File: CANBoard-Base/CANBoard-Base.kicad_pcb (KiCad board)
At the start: 4 copper layers, 62.2 x 73.8 mm, 110 parts, among them J1 DTM12 A, J2 DTM12 B, U1 CANBoard_v2, U2 LM324, U3 LM324, U4 SRV05-4, U5 SRV05-4, U6 SRV05-4, U7 SRV05-4, U8 LD1117S33CTR

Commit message: version 1.1 ready for manuf
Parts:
- moved R13 34.8 mm to (3.81, -30.8), turned to 90 degrees
- moved JP5 34.3 mm to (6.10, -30.8), turned to 90 degrees
- moved R12 33.6 mm to (8.38, -30.8), turned to 90 degrees
- moved JP4 33.3 mm to (10.7, -30.8), turned to 90 degrees
- moved R14 31.9 mm to (3.81, -34.4)
- moved JP10 31.4 mm to (6.10, -34.5), turned to -90 degrees
- moved R15 30.6 mm to (8.38, -34.4)
- moved JP9 30.2 mm to (10.7, -34.5), turned to -90 degrees
- moved R11 21.1 mm to (3.81, -21.3), turned to 90 degrees
- moved JP3 20.7 mm to (6.10, -21.3), turned to 90 degrees
- moved R16 20.6 mm to (3.81, -24.9)
- moved R10 20.1 mm to (8.38, -21.3), turned to 90 degrees
- moved JP8 20.0 mm to (6.10, -24.9), turned to -90 degrees
- moved JP2 19.7 mm to (10.7, -21.3), turned to 90 degrees
- moved R17 19.6 mm to (8.38, -24.9)
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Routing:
- net AI4_RAW: track 19.5 -> 45.8 mm
- net AI5_RAW: track 21.8 -> 45.2 mm
- net AI1_RAW: track 20.2 -> 32.1 mm
- net AI2_RAW: track 18.9 -> 30.5 mm
- net AI3_RAW: track 18.6 -> 28.9 mm
- net +5VP: track 16.1 -> 8.48 mm
- net +5V: track 55.4 -> 56.4 mm
- net Net-(JP9-A): track 2.35 -> 2.99 mm
- net Net-(JP8-A): track 2.35 -> 2.93 mm
- net Net-(JP6-A): track 2.35 -> 2.93 mm
- net Net-(JP7-A): track 2.35 -> 2.93 mm
- net Net-(JP10-A): track 2.47 -> 2.98 mm
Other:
- board text added: "1"
- board text added: "2"
- board text added: "3"
- board text added: "4"
- board text added: "5"
- board text added: "ANALOG INPUTS"
- board text added: "DIGITAL INPUTS"
- board text added: "PD"
- board text added: "PU"
- board text removed: "5|4|3|2|1"

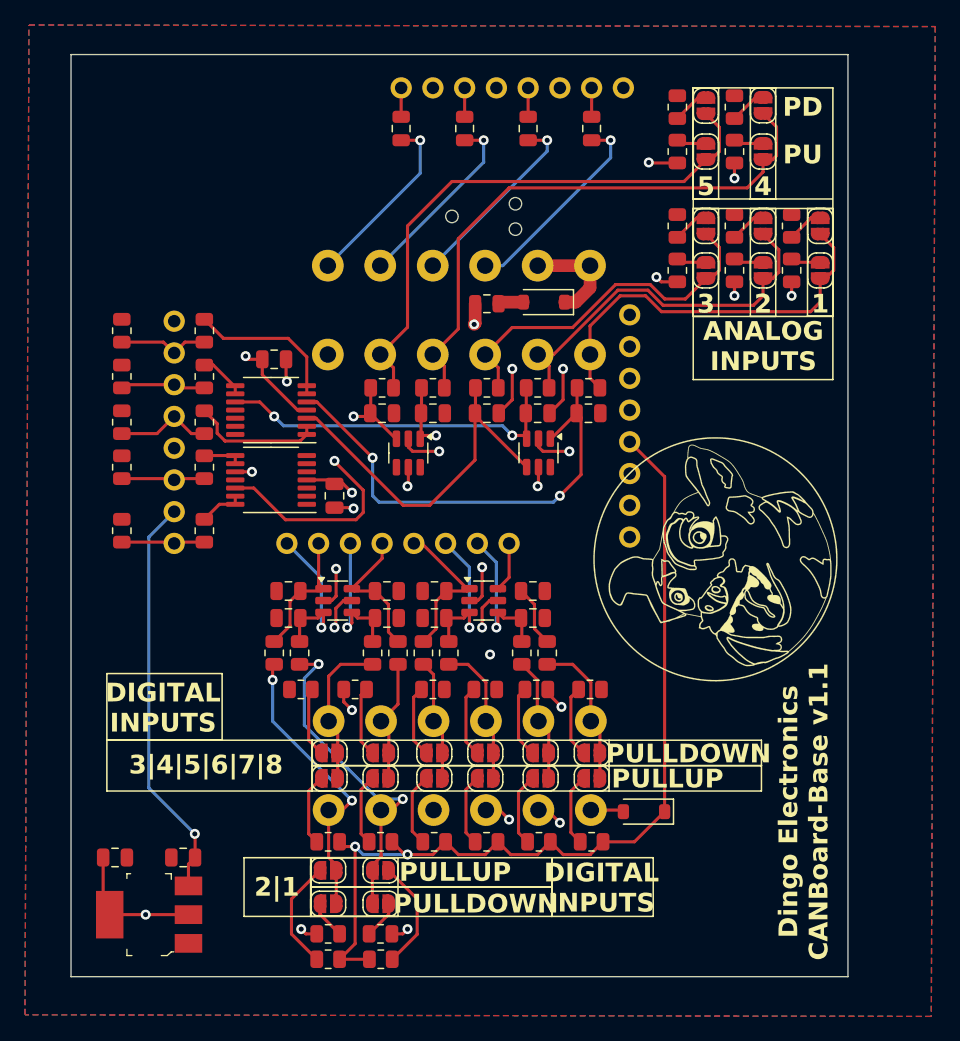
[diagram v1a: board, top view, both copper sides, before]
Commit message: change to mcp6004
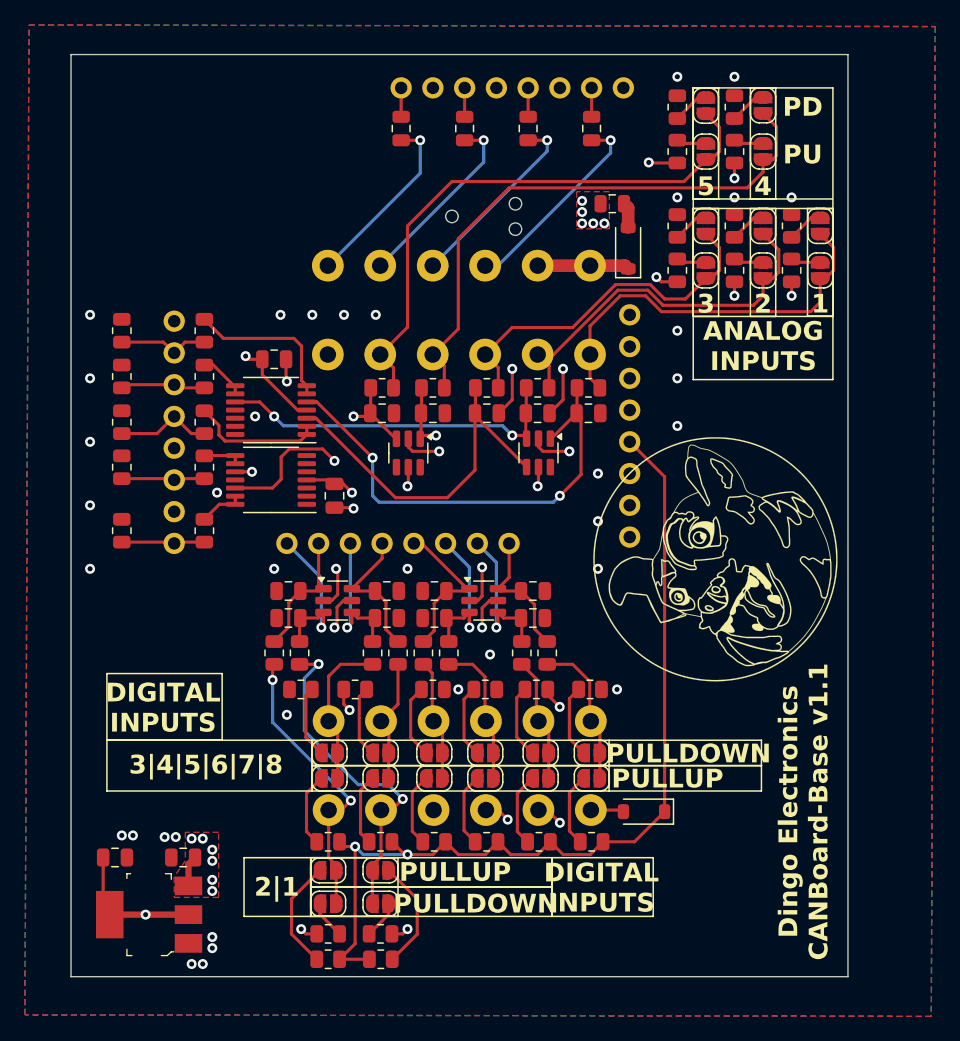
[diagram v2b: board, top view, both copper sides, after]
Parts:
- U2, U3: value LM324 -> MCP6004
- moved F1 12.8 mm to (-1.40, -26.7)
- moved D2 8.00 mm to (-0.13, -23.1), turned to 90 degrees
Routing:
- net +5V: track 56.4 -> 24.7 mm, vias 11 -> 20
- net Net-(U3D-+): track 27.2 -> 21.3 mm
- net /DigitalInputs/DI8: track 9.17 -> 10.8 mm
- net +5VP: track 8.48 -> 7.34 mm
- net GND: vias 13 -> 48
- added copper zone on F.Cu, net +5V
